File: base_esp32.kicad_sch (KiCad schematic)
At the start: 77 parts, among them J1 Input Source, J10 H_IO15_OUT, J11 H_IO32_OUT, J12 H_IO02_OUT, J13 H_IO04_OUT, J14 5V, J15 5V, J16 H_3V3_1, J17 H_IO34, J18 H_IO35, J19 H_IO36, J2 BYPASS_SRC_5V, J20 H_IO39, J21 S_3V3_1, J22 H_3V3_2, J23 H_KEYPAD, J24 H_I2C, J25 H_SPI, J26 TX_RX, J27 S_3V3_2, J28 H_GND, J29 S_KEYPAD, J3 BYPASS_SRC_3V3, J30 S_I2C, J31 S_SPI, J32 S_GND, J33 Src Board, J4 H_IO33, J5 H_IO15, J6 H_IO32, J7 H_IO02, J8 H_IO04, J9 H_IO33_OUT, SW1 INPUT_D1, SW2 INPUT_D2, SW3 SW_DIP_INPUTS, SW4 ENABLE, SW5 SW_DIP_KEYPAD, SW6 Selector_Input, SW7 Selector_Input, SW8 BOOT, U1 LM7805_TO220, U2 AMS1117, U3 AMS1117, U4 ESP32-DevKitC

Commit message: fix: package to sw5 dip
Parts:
- SW5: footprint Button_Switch_THT:SW_DIP_SPSTx04_Slide_9.78x12.34mm_W7.62mm_P2.54mm -> Button_Switch_THT:SW_DIP_SPSTx08_Slide_9.78x22.5mm_W7.62mm_P2.54mm
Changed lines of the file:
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@@
 			)
 		)
-		(property "Footprint" "Button_Switch_THT:SW_DIP_SPSTx04_Slide_9.78x12.34mm_W7.62mm_P2.54mm"
+		(property "Footprint" "Button_Switch_THT:SW_DIP_SPSTx08_Slide_9.78x22.5mm_W7.62mm_P2.54mm"
 			(at 129.54 62.23 0)
 			(effects

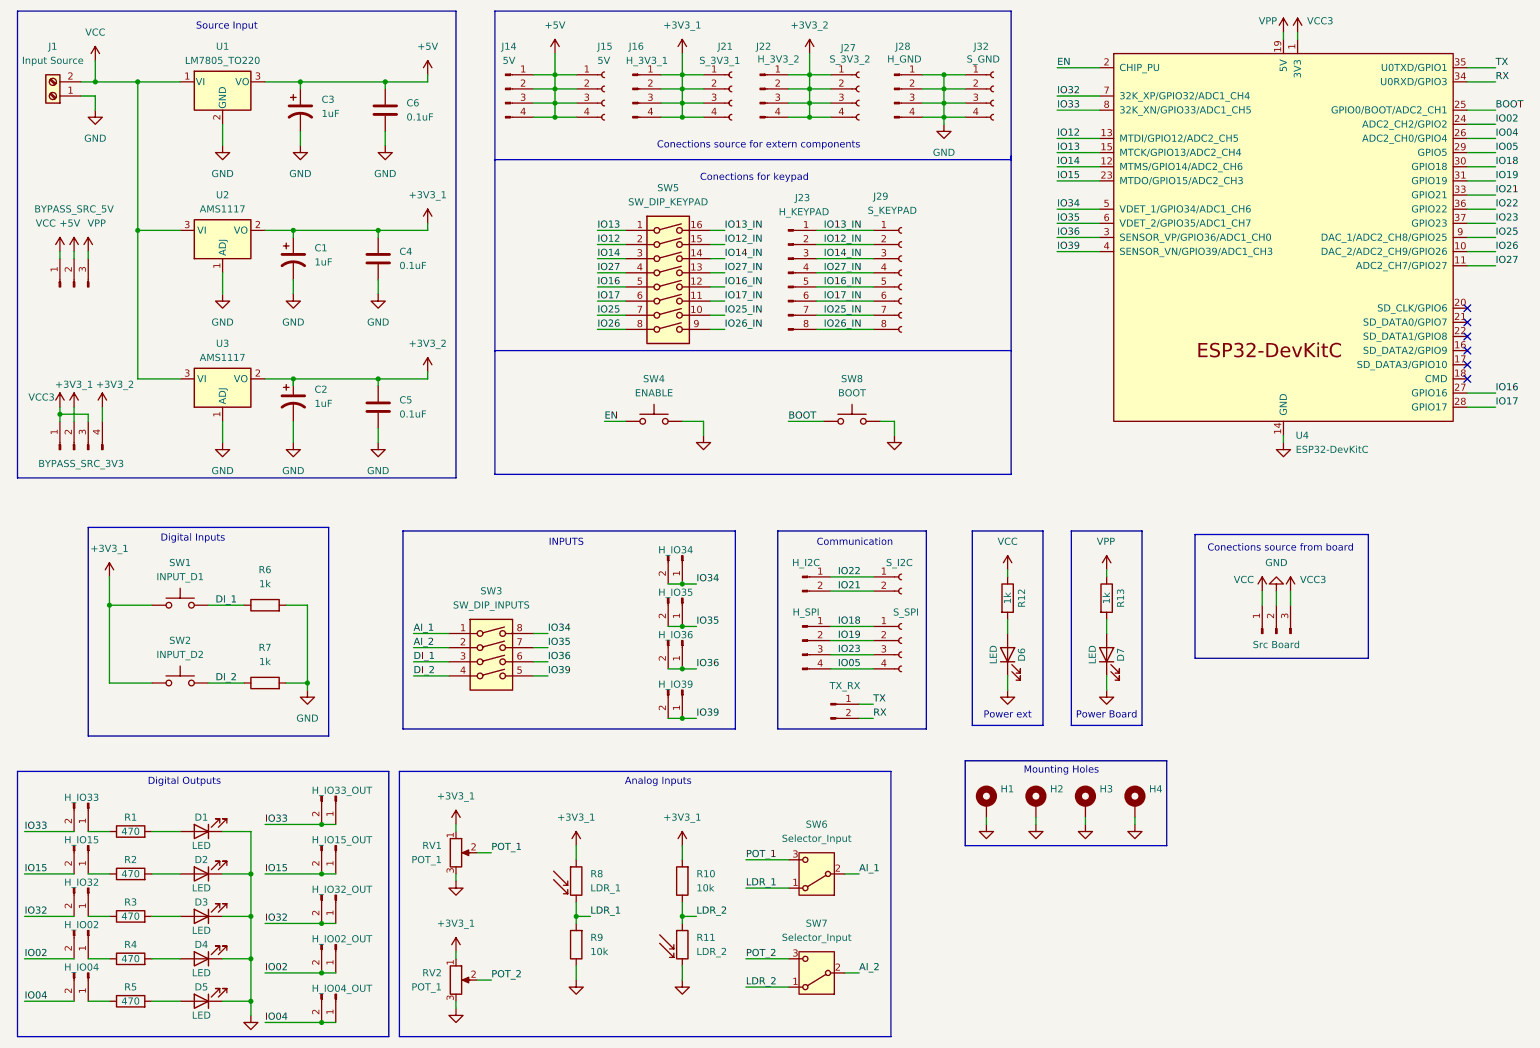
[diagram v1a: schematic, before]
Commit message: fix: footprints
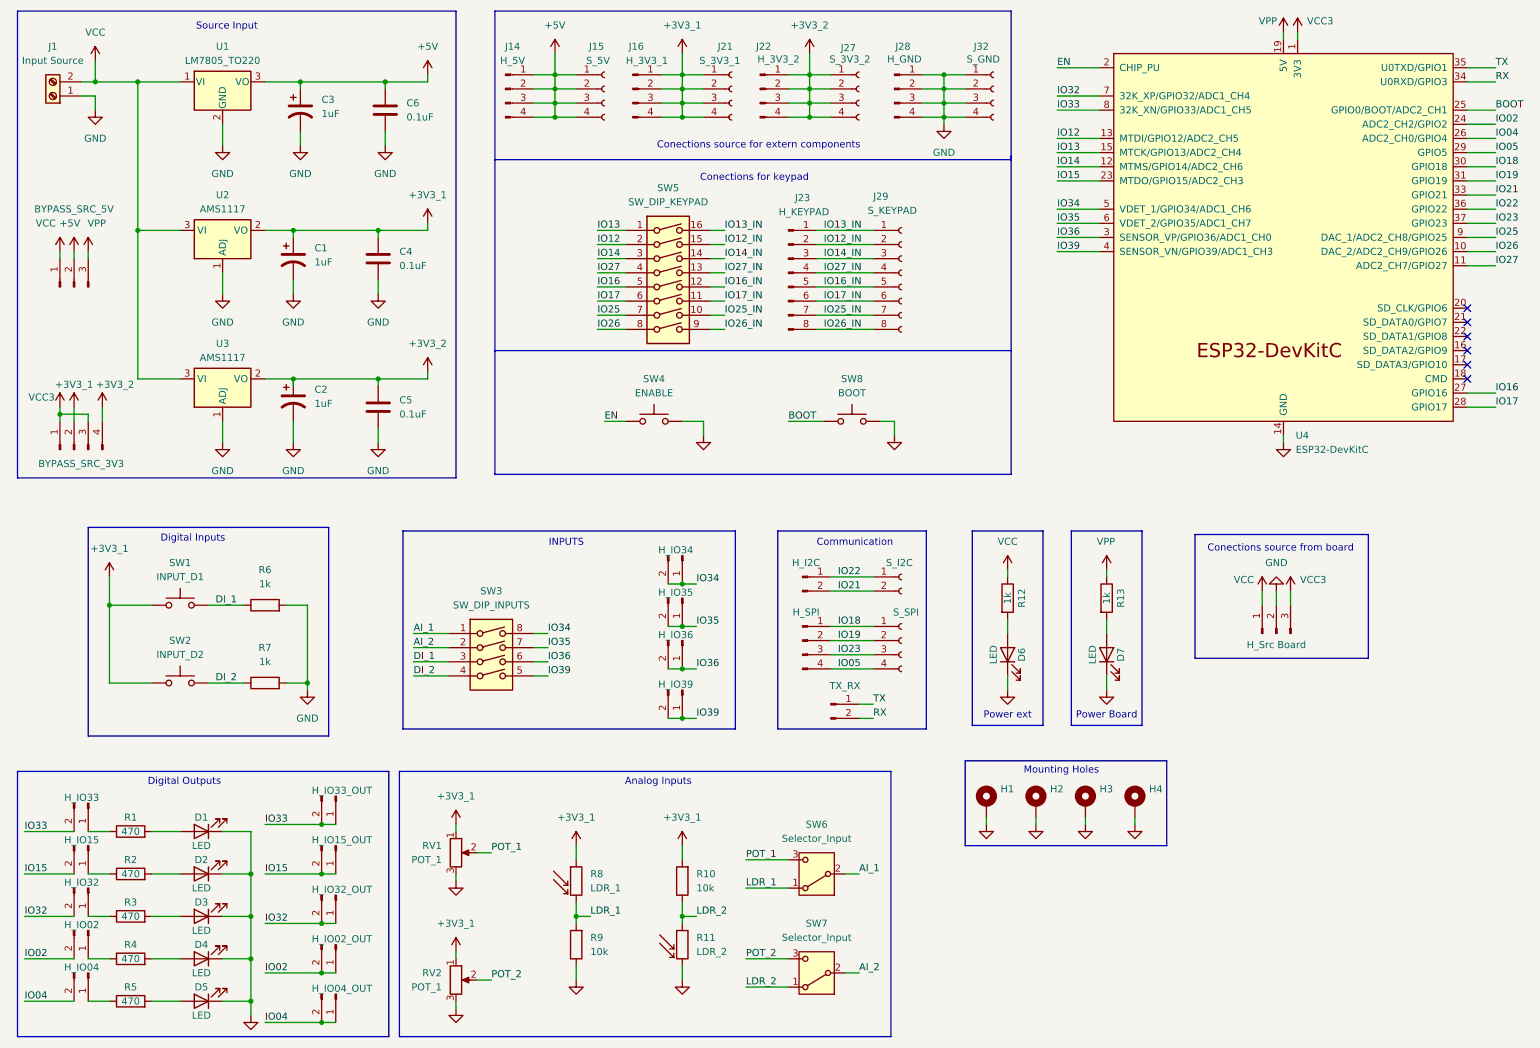
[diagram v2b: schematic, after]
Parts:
- J1: footprint TerminalBlock:TerminalBlock_Xinya_XY308-2.54-2P_1x02_P2.54mm_Horizontal -> TerminalBlock_Phoenix:TerminalBlock_Phoenix_PT-1,5-2-5.0-H_1x02_P5.00mm_Horizontal
- J10, J11, J12, J13, J17, J18, J19, J20, J24, J26, J4, J5, J6, J7, J8, J9: footprint Connector_PinHeader_1.27mm:PinHeader_1x02_P1.27mm_Vertical -> Connector_PinHeader_2.54mm:PinHeader_1x02_P2.54mm_Vertical
- J14: value 5V -> H_5V; footprint Connector_PinHeader_1.27mm:PinHeader_1x04_P1.27mm_Vertical -> Connector_PinHeader_2.54mm:PinHeader_1x04_P2.54mm_Vertical
- J15: value 5V -> S_5V; footprint Connector_PinSocket_1.27mm:PinSocket_1x04_P1.27mm_Vertical -> Connector_PinSocket_2.54mm:PinSocket_1x04_P2.54mm_Vertical
- J16, J22, J25, J28: footprint Connector_PinHeader_1.27mm:PinHeader_1x04_P1.27mm_Vertical -> Connector_PinHeader_2.54mm:PinHeader_1x04_P2.54mm_Vertical
- J2: footprint Connector_PinHeader_1.27mm:PinHeader_1x03_P1.27mm_Vertical -> Connector_PinHeader_2.54mm:PinHeader_1x03_P2.54mm_Vertical
- J21, J27, J31, J32: footprint Connector_PinSocket_1.27mm:PinSocket_1x04_P1.27mm_Vertical -> Connector_PinSocket_2.54mm:PinSocket_1x04_P2.54mm_Vertical
- J23: footprint Connector_PinHeader_1.27mm:PinHeader_1x08_P1.27mm_Vertical -> Connector_PinHeader_2.54mm:PinHeader_1x08_P2.54mm_Vertical
- J29: footprint Connector_PinSocket_1.27mm:PinSocket_1x08_P1.27mm_Vertical -> Connector_PinSocket_2.54mm:PinSocket_1x08_P2.54mm_Vertical
- J3: footprint Connector_PinHeader_1.00mm:PinHeader_1x04_P1.00mm_Vertical -> Connector_PinHeader_2.54mm:PinHeader_1x04_P2.54mm_Vertical
- J30: footprint Connector_PinSocket_1.27mm:PinSocket_1x02_P1.27mm_Vertical -> Connector_PinSocket_2.54mm:PinSocket_1x02_P2.54mm_Vertical
- J33: value Src Board -> H_Src Board; footprint Connector_PinHeader_1.27mm:PinHeader_1x03_P1.27mm_Vertical -> Connector_PinHeader_2.54mm:PinHeader_1x03_P2.54mm_Vertical
- SW6, SW7: footprint Button_Switch_THT:SW_Slide-03_Wuerth-WS-SLTV_10x2.5x6.4_P2.54mm -> Connector_PinHeader_2.54mm:PinHeader_1x03_P2.54mm_Vertical
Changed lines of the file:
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@@
 			)
 		)
-		(property "Footprint" "Connector_PinHeader_1.27mm:PinHeader_1x02_P1.27mm_Vertical"
+		(property "Footprint" "Connector_PinHeader_2.54mm:PinHeader_1x02_P2.54mm_Vertical"
 			(at 158.75 137.16 0)
 			(effects
@@
 			)
 		)
-		(property "Footprint" "Connector_PinHeader_1.27mm:PinHeader_1x04_P1.27mm_Vertical"
+		(property "Footprint" "Connector_PinHeader_2.54mm:PinHeader_1x04_P2.54mm_Vertical"
 			(at 146.05 26.67 0)
 			(effects
@@
 			)
 		)
-		(property "Footprint" "Connector_PinSocket_1.27mm:PinSocket_1x04_P1.27mm_Vertical"
+		(property "Footprint" "Connector_PinSocket_2.54mm:PinSocket_1x04_P2.54mm_Vertical"
 			(at 163.83 26.67 0)
 			(effects
@@
 			)
 		)
-		(property "Value" "Src Board"
+		(property "Value" "H_Src Board"
 			(at 238.76 126.492 90)
 			(effects
@@
 			)
 		)
-		(property "Footprint" "Connector_PinHeader_1.27mm:PinHeader_1x03_P1.27mm_Vertical"
+		(property "Footprint" "Connector_PinHeader_2.54mm:PinHeader_1x03_P2.54mm_Vertical"
 			(at 238.76 124.46 0)
 			(effects
@@
 			)
 		)
-		(property "Footprint" "Connector_PinHeader_1.27mm:PinHeader_1x02_P1.27mm_Vertical"
+		(property "Footprint" "Connector_PinHeader_2.54mm:PinHeader_1x02_P2.54mm_Vertical"
 			(at 25.4 162.56 0)
 			(effects
@@
 			)
 		)
-		(property "Footprint" "Connector_PinHeader_1.00mm:PinHeader_1x04_P1.00mm_Vertical"
+		(property "Footprint" "Connector_PinHeader_2.54mm:PinHeader_1x04_P2.54mm_Vertical"
 			(at 22.86 91.44 0)
 			(effects
@@
 			)
 		)
-		(property "Footprint" "Connector_PinHeader_1.27mm:PinHeader_1x04_P1.27mm_Vertical"
+		(property "Footprint" "Connector_PinHeader_2.54mm:PinHeader_1x04_P2.54mm_Vertical"
 			(at 153.67 125.73 0)
 			(effects
@@
 			)
 		)
-		(property "Footprint" "Connector_PinHeader_1.27mm:PinHeader_1x04_P1.27mm_Vertical"
+		(property "Footprint" "Connector_PinHeader_2.54mm:PinHeader_1x04_P2.54mm_Vertical"
 			(at 170.18 26.67 0)
 			(effects
@@
 			)
 		)
-		(property "Footprint" "Connector_PinSocket_1.27mm:PinSocket_1x04_P1.27mm_Vertical"
+		(property "Footprint" "Connector_PinSocket_2.54mm:PinSocket_1x04_P2.54mm_Vertical"
 			(at 187.96 26.67 0)
 			(effects
@@
 			)
 		)
-		(property "Footprint" "Connector_PinHeader_1.27mm:PinHeader_1x02_P1.27mm_Vertical"
+		(property "Footprint" "Connector_PinHeader_2.54mm:PinHeader_1x02_P2.54mm_Vertical"
 			(at 25.4 170.18 0)
 			(effects
@@
 			)
 		)
-		(property "Footprint" "Connector_PinHeader_1.27mm:PinHeader_1x02_P1.27mm_Vertical"
+		(property "Footprint" "Connector_PinHeader_2.54mm:PinHeader_1x02_P2.54mm_Vertical"
 			(at 132.08 118.11 0)
 			(effects
@@
 			)
 		)
-		(property "Footprint" "Connector_PinHeader_1.27mm:PinHeader_1x02_P1.27mm_Vertical"
+		(property "Footprint" "Connector_PinHeader_2.54mm:PinHeader_1x02_P2.54mm_Vertical"
 			(at 69.85 189.23 0)
 			(effects
@@
 			)
 		)
-		(property "Footprint" "Connector_PinHeader_1.27mm:PinHeader_1x03_P1.27mm_Vertical"
+		(property "Footprint" "Connector_PinHeader_2.54mm:PinHeader_1x03_P2.54mm_Vertical"
 			(at 22.86 62.23 0)
 			(effects
@@
 			)
 		)
-		(property "Footprint" "Connector_PinHeader_1.27mm:PinHeader_1x02_P1.27mm_Vertical"
+		(property "Footprint" "Connector_PinHeader_2.54mm:PinHeader_1x02_P2.54mm_Vertical"
 			(at 69.85 180.34 0)
 			(effects
@@
 			)
 		)
-		(property "Footprint" "Connector_PinSocket_1.27mm:PinSocket_1x04_P1.27mm_Vertical"
+		(property "Footprint" "Connector_PinSocket_2.54mm:PinSocket_1x04_P2.54mm_Vertical"
 			(at 140.97 26.67 0)
 			(effects
@@
 			)
 		)
-		(property "Footprint" "Connector_PinHeader_1.27mm:PinHeader_1x02_P1.27mm_Vertical"
+		(property "Footprint" "Connector_PinHeader_2.54mm:PinHeader_1x02_P2.54mm_Vertical"
 			(at 69.85 153.67 0)
 			(effects
@@
 		(on_board yes)
 		(dnp no)
-		(fields_autoplaced yes)
 		(property "Reference" "J14"
-			(at 100.965 19.05 0)
+			(at 101.6 19.05 0)
 			(effects
 				(font
@@
 			)
 		)
-		(property "Value" "5V"
-			(at 100.965 21.59 0)
+		(property "Value" "H_5V"
+			(at 101.6 21.59 0)
 			(effects
 				(font
@@
 			)
 		)
-		(property "Footprint" "Connector_PinHeader_1.27mm:PinHeader_1x04_P1.27mm_Vertical"
+		(property "Footprint" "Connector_PinHeader_2.54mm:PinHeader_1x04_P2.54mm_Vertical"
 			(at 100.33 26.67 0)
 			(effects
@@
 			)
 		)
-		(property "Footprint" "Connector_PinHeader_1.27mm:PinHeader_1x04_P1.27mm_Vertical"
+		(property "Footprint" "Connector_PinHeader_2.54mm:PinHeader_1x04_P2.54mm_Vertical"
 			(at 123.19 26.67 0)
 			(effects
@@
 			)
 		)
-		(property "Footprint" "Connector_PinHeader_1.27mm:PinHeader_1x02_P1.27mm_Vertical"
+		(property "Footprint" "Connector_PinHeader_2.54mm:PinHeader_1x02_P2.54mm_Vertical"
 			(at 132.08 134.62 0)
 			(effects
@@
 			)
 		)
-		(property "Footprint" "Connector_PinHeader_1.27mm:PinHeader_1x02_P1.27mm_Vertical"
+		(property "Footprint" "Connector_PinHeader_2.54mm:PinHeader_1x02_P2.54mm_Vertical"
 			(at 153.67 114.3 0)
 			(effects
@@
 			)
 		)
-		(property "Footprint" "Connector_PinSocket_1.27mm:PinSocket_1x08_P1.27mm_Vertical"
+		(property "Footprint" "Connector_PinSocket_2.54mm:PinSocket_1x08_P2.54mm_Vertical"
 			(at 171.45 59.69 0)
 			(effects
@@
 			)
 		)
-		(property "Footprint" "Connector_PinHeader_1.27mm:PinHeader_1x02_P1.27mm_Vertical"
+		(property "Footprint" "Connector_PinHeader_2.54mm:PinHeader_1x02_P2.54mm_Vertical"
 			(at 25.4 154.94 0)
 			(effects
@@
 			)
 		)
-		(property "Footprint" "Connector_PinSocket_1.27mm:PinSocket_1x04_P1.27mm_Vertical"
+		(property "Footprint" "Connector_PinSocket_2.54mm:PinSocket_1x04_P2.54mm_Vertical"
 			(at 171.45 125.73 0)
 			(effects
@@
 			)
 		)
-		(property "Footprint" "TerminalBlock:TerminalBlock_Xinya_XY308-2.54-2P_1x02_P2.54mm_Horizontal"
+		(property "Footprint" "TerminalBlock_Phoenix:TerminalBlock_Phoenix_PT-1,5-2-5.0-H_1x02_P5.00mm_Horizontal"
 			(at 19.05 27.94 0)
 			(effects
@@
 			)
 		)
-		(property "Footprint" "Connector_PinHeader_1.27mm:PinHeader_1x02_P1.27mm_Vertical"
+		(property "Footprint" "Connector_PinHeader_2.54mm:PinHeader_1x02_P2.54mm_Vertical"
 			(at 25.4 185.42 0)
 			(effects
@@
 			)
 		)
-		(property "Footprint" "Connector_PinHeader_1.27mm:PinHeader_1x08_P1.27mm_Vertical"
+		(property "Footprint" "Connector_PinHeader_2.54mm:PinHeader_1x08_P2.54mm_Vertical"
 			(at 151.13 59.69 0)
 			(effects
@@
 			)
 		)
-		(property "Footprint" "Connector_PinHeader_1.27mm:PinHeader_1x02_P1.27mm_Vertical"
+		(property "Footprint" "Connector_PinHeader_2.54mm:PinHeader_1x02_P2.54mm_Vertical"
 			(at 69.85 171.45 0)
 			(effects
@@
 			)
 		)
-		(property "Footprint" "Connector_PinHeader_1.27mm:PinHeader_1x02_P1.27mm_Vertical"
+		(property "Footprint" "Connector_PinHeader_2.54mm:PinHeader_1x02_P2.54mm_Vertical"
 			(at 132.08 110.49 0)
 			(effects
@@
 			)
 		)
-		(property "Footprint" "Button_Switch_THT:SW_Slide-03_Wuerth-WS-SLTV_10x2.5x6.4_P2.54mm"
+		(property "Footprint" "Connector_PinHeader_2.54mm:PinHeader_1x03_P2.54mm_Vertical"
 			(at 156.21 167.64 0)
 			(effects
@@
 			)
 		)
-		(property "Footprint" "Connector_PinSocket_1.27mm:PinSocket_1x02_P1.27mm_Vertical"
+		(property "Footprint" "Connector_PinSocket_2.54mm:PinSocket_1x02_P2.54mm_Vertical"
 			(at 171.45 114.3 0)
 			(effects
@@
 			)
 		)
-		(property "Footprint" "Connector_PinHeader_1.27mm:PinHeader_1x02_P1.27mm_Vertical"
+		(property "Footprint" "Connector_PinHeader_2.54mm:PinHeader_1x02_P2.54mm_Vertical"
 			(at 25.4 177.8 0)
 			(effects
@@
 			)
 		)
-		(property "Footprint" "Connector_PinHeader_1.27mm:PinHeader_1x02_P1.27mm_Vertical"
+		(property "Footprint" "Connector_PinHeader_2.54mm:PinHeader_1x02_P2.54mm_Vertical"
 			(at 132.08 125.73 0)
 			(effects
@@
 			)
 		)
-		(property "Footprint" "Button_Switch_THT:SW_Slide-03_Wuerth-WS-SLTV_10x2.5x6.4_P2.54mm"
+		(property "Footprint" "Connector_PinHeader_2.54mm:PinHeader_1x03_P2.54mm_Vertical"
 			(at 156.21 185.42 0)
 			(effects
@@
 		(dnp no)
 		(property "Reference" "J15"
-			(at 116.84 19.05 0)
+			(at 115.316 19.05 0)
 			(effects
 				(font
@@
 			)
 		)
-		(property "Value" "5V"
-			(at 116.84 21.59 0)
+		(property "Value" "S_5V"
+			(at 114.808 21.59 0)
 			(effects
 				(font
@@
 			)
 		)
-		(property "Footprint" "Connector_PinSocket_1.27mm:PinSocket_1x04_P1.27mm_Vertical"
+		(property "Footprint" "Connector_PinSocket_2.54mm:PinSocket_1x04_P2.54mm_Vertical"
 			(at 118.11 26.67 0)
 			(effects
@@
 			)
 		)
-		(property "Footprint" "Connector_PinHeader_1.27mm:PinHeader_1x02_P1.27mm_Vertical"
+		(property "Footprint" "Connector_PinHeader_2.54mm:PinHeader_1x02_P2.54mm_Vertical"
 			(at 69.85 162.56 0)
 			(effects

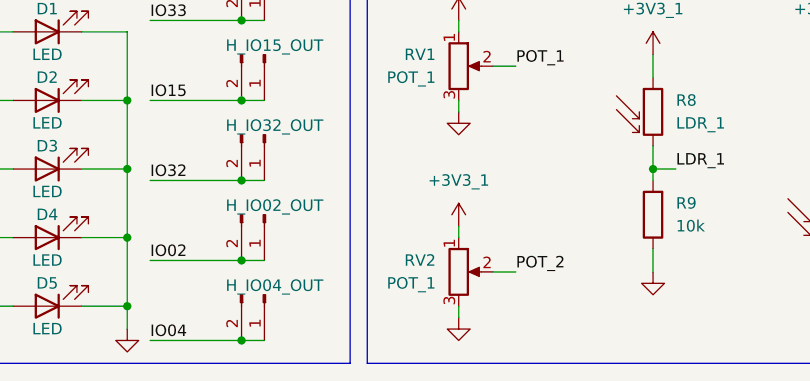
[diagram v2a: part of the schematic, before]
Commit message: fix: pot2 and change footprint
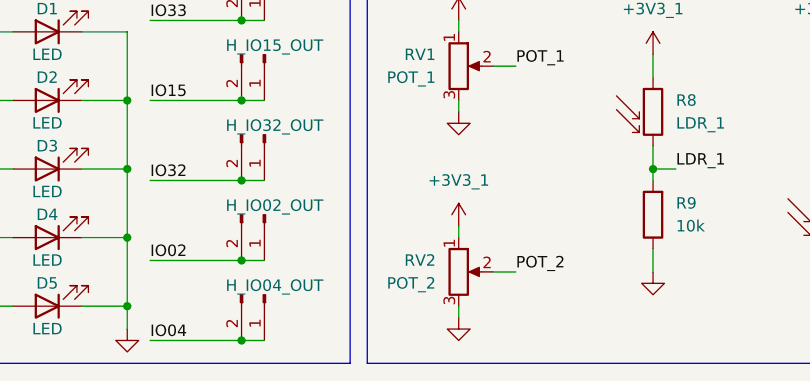
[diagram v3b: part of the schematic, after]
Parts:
- RV2: value POT_1 -> POT_2; footprint Potentiometer_THT:Potentiometer_Alps_RK163_Single_Horizontal -> Potentiometer_THT:Potentiometer_Piher_PT-10-V05_Vertical
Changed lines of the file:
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@@
 			)
 		)
-		(property "Value" "POT_1"
+		(property "Value" "POT_2"
 			(at 88.9 187.9599 0)
 			(effects
@@
 			)
 		)
-		(property "Footprint" "Potentiometer_THT:Potentiometer_Alps_RK163_Single_Horizontal"
+		(property "Footprint" "Potentiometer_THT:Potentiometer_Piher_PT-10-V05_Vertical"
 			(at 91.44 186.69 0)
 			(effects

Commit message: fix: some tags for pcb, sorting elements
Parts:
- D6: value LED -> LED EXT
- D7: value LED -> LED BOARD
- J2: value BYPASS_SRC_5V -> BYPASS SRC 5V
- J3: value BYPASS_SRC_3V3 -> BYPASS SRC 3V3
- SW6: value Selector_Input -> Selector Input 1
- SW7: value Selector_Input -> Selector Input 2
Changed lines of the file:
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@@
 			)
 		)
-		(property "Value" "BYPASS_SRC_3V3"
+		(property "Value" "BYPASS SRC 3V3"
 			(at 24.13 93.98 90)
 			(effects
@@
 			)
 		)
-		(property "Value" "BYPASS_SRC_5V"
+		(property "Value" "BYPASS SRC 5V"
 			(at 22.86 48.26 90)
 			(effects
@@
 			)
 		)
-		(property "Value" "LED"
+		(property "Value" "LED EXT"
 			(at 187.96 128.27 0)
 			(effects
@@
 			)
 		)
-		(property "Value" "LED"
+		(property "Value" "LED BOARD"
 			(at 205.74 128.27 0)
 			(effects
@@
 			)
 		)
-		(property "Value" "Selector_Input"
+		(property "Value" "Selector Input 1"
 			(at 156.21 161.29 0)
 			(effects
@@
 			)
 		)
-		(property "Value" "Selector_Input"
+		(property "Value" "Selector Input 2"
 			(at 156.21 179.07 0)
 			(effects
